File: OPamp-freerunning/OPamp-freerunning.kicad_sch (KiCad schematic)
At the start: 5 parts, among them U1 ${SIM.PARAMS}

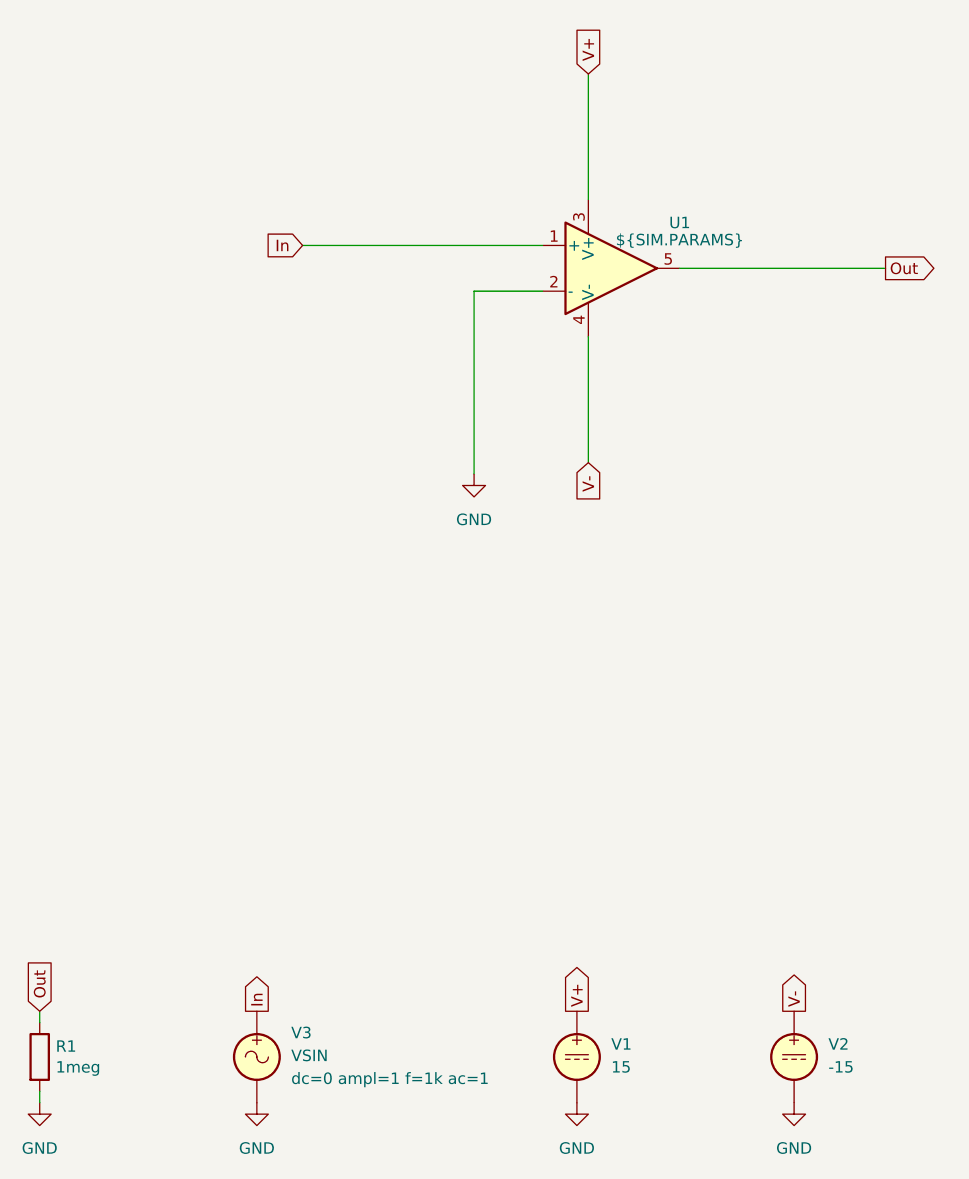
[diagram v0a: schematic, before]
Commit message: Tested/updated for KiCad 9
Schematics are tested and updated for KiCad 9, no changes in circuitry
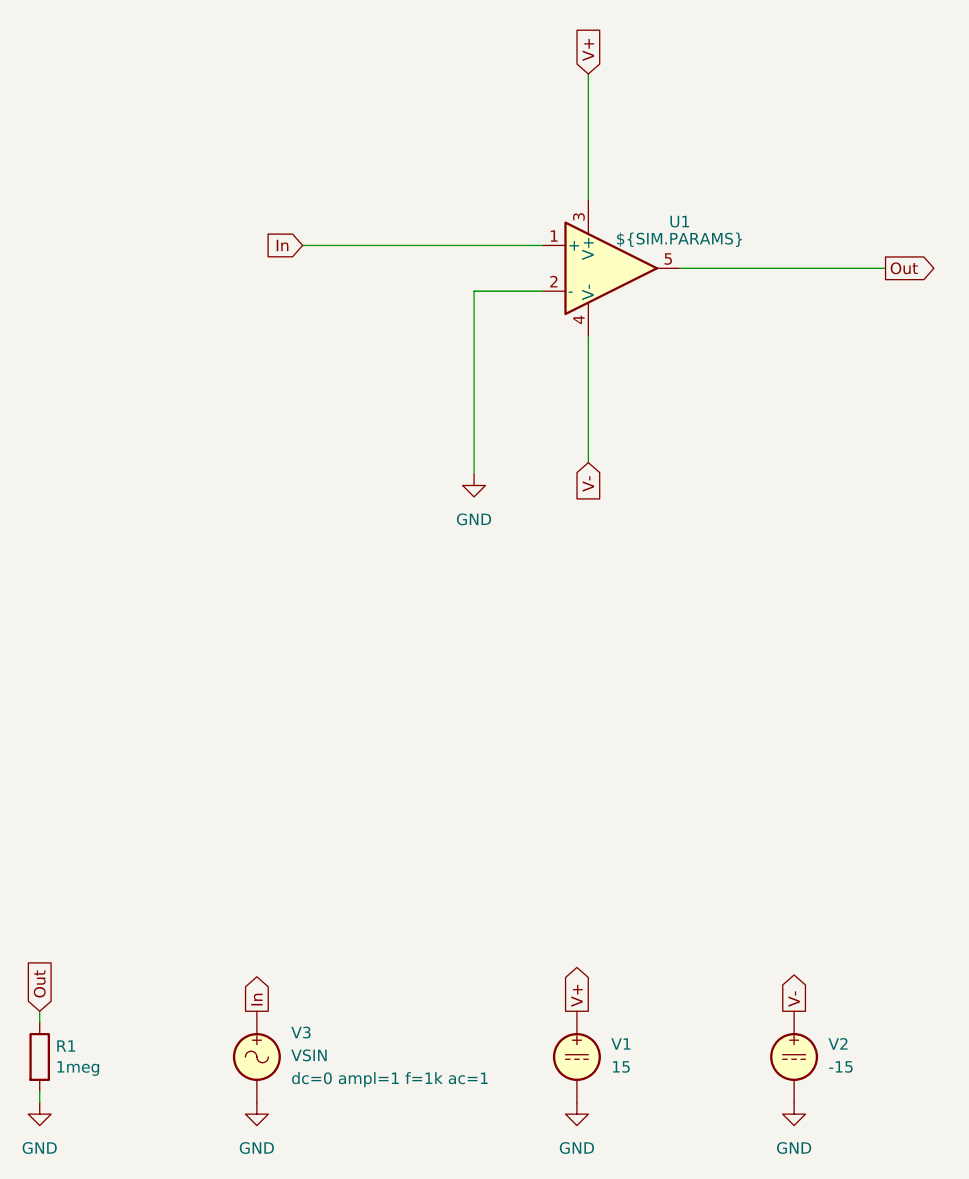
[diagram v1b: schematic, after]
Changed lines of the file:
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@@
 (kicad_sch
-	(version 20231120)
+	(version 20250114)
 	(generator "eeschema")
-	(generator_version "8.0")
+	(generator_version "9.0")
 	(paper "A4")
 	(title_block
 		(title "OPamp, freerunning")
-		(date "2024-12-15")
+		(date "2025-09-13")
 		(company "GitHub/OJStuff")
 		(comment 4 "Does not work properly at the time (probably built-in SPICE model problems)")
@@
 	)
 	(symbol
-		(lib_id "Simulation_SPICE:OPAMP")
-		(at 139.7 93.98 0)
-		(unit 1)
-		(exclude_from_sim no)
-		(in_bom yes)
-		(on_board yes)
-		(dnp no)
-		(fields_autoplaced yes)
-		(property "Reference" "U1"
-			(at 147.32 88.9314 0)
-			(effects
-				(font
-					(size 1.27 1.27)
-				)
-			)
-		)
-		(property "Value" "${SIM.PARAMS}"
-			(at 147.32 90.8365 0)
-			(effects
-				(font
-					(size 1.27 1.27)
-				)
-			)
-		)
-		(property "Footprint" ""
-			(at 139.7 93.98 0)
-			(effects
-				(font
-					(size 1.27 1.27)
-				)
-				(hide yes)
-			)
-		)
-		(property "Datasheet" "https://ngspice.sourceforge.io/docs/ngspice-html-manual/manual.xhtml#sec__SUBCKT_Subcircuits"
-			(at 139.7 93.98 0)
-			(effects
-				(font
-					(size 1.27 1.27)
-				)
-				(hide yes)
-			)
-		)
-		(property "Description" "Operational amplifier, single, node sequence=1:+ 2:- 3:OUT 4:V+ 5:V-"
-			(at 139.7 93.98 0)
-			(effects
-				(font
-					(size 1.27 1.27)
-				)
-				(hide yes)
-			)
-		)
-		(property "Sim.Pins" "1=in+ 2=in- 3=vcc 4=vee 5=out"
-			(at 139.7 93.98 0)
-			(effects
-				(font
-					(size 1.27 1.27)
-				)
-				(hide yes)
-			)
-		)
-		(property "Sim.Device" "SUBCKT"
-			(at 139.7 93.98 0)
-			(effects
-				(font
-					(size 1.27 1.27)
-				)
-				(justify left)
-				(hide yes)
-			)
-		)
-		(property "Sim.Library" "${KICAD8_SYMBOL_DIR}/Simulation_SPICE.sp"
-			(at 139.7 93.98 0)
-			(effects
-				(font
-					(size 1.27 1.27)
-				)
-				(hide yes)
-			)
-		)
-		(property "Sim.Name" "kicad_builtin_opamp"
-			(at 139.7 93.98 0)
-			(effects
-				(font
-					(size 1.27 1.27)
-				)
-				(hide yes)
-			)
-		)
-		(pin "2"
-		)
-		(pin "1"
-		)
-		(pin "5"
-		)
-		(pin "3"
-		)
-		(pin "4"
-		)
-		(instances
-			(project ""
-				(path "/d4e8d3f6-5bf3-42e6-a3b5-7574d3319bb2"
-					(reference "U1")
-					(unit 1)
-				)
-			)
-		)
-	)
-	(symbol
 		(lib_name "VDC_1")
 		(lib_id "Simulation_SPICE:VDC")
@@
 				(path "/d4e8d3f6-5bf3-42e6-a3b5-7574d3319bb2"
 					(reference "#PWR01")
+					(unit 1)
+				)
+			)
+		)
+	)
+	(symbol
+		(lib_id "Simulation_SPICE:OPAMP")
+		(at 139.7 93.98 0)
+		(unit 1)
+		(exclude_from_sim no)
+		(in_bom yes)
+		(on_board yes)
+		(dnp no)
+		(fields_autoplaced yes)
+		(property "Reference" "U1"
+			(at 147.32 88.8298 0)
+			(effects
+				(font
+					(size 1.27 1.27)
+				)
+			)
+		)
+		(property "Value" "${SIM.PARAMS}"
+			(at 147.32 90.7349 0)
+			(effects
+				(font
+					(size 1.27 1.27)
+				)
+			)
+		)
+		(property "Footprint" ""
+			(at 139.7 93.98 0)
+			(effects
+				(font
+					(size 1.27 1.27)
+				)
+				(hide yes)
+			)
+		)
+		(property "Datasheet" "https://ngspice.sourceforge.io/docs/ngspice-html-manual/manual.xhtml#sec__SUBCKT_Subcircuits"
+			(at 139.7 93.98 0)
+			(effects
+				(font
+					(size 1.27 1.27)
+				)
+				(hide yes)
+			)
+		)
+		(property "Description" "Operational amplifier, single"
+			(at 139.7 93.98 0)
+			(effects
+				(font
+					(size 1.27 1.27)
+				)
+				(hide yes)
+			)
+		)
+		(property "Sim.Pins" "1=in+ 2=in- 3=vcc 4=vee 5=out"
+			(at 139.7 93.98 0)
+			(effects
+				(font
+					(size 1.27 1.27)
+				)
+				(hide yes)
+			)
+		)
+		(property "Sim.Device" "SUBCKT"
+			(at 139.7 93.98 0)
+			(effects
+				(font
+					(size 1.27 1.27)
+				)
+				(justify left)
+				(hide yes)
+			)
+		)
+		(property "Sim.Library" "${KICAD9_SYMBOL_DIR}/Simulation_SPICE.sp"
+			(at 139.7 93.98 0)
+			(effects
+				(font
+					(size 1.27 1.27)
+				)
+				(hide yes)
+			)
+		)
+		(property "Sim.Name" "kicad_builtin_opamp"
+			(at 139.7 93.98 0)
+			(effects
+				(font
+					(size 1.27 1.27)
+				)
+				(hide yes)
+			)
+		)
+		(pin "5"
+		)
+		(pin "4"
+		)
+		(pin "3"
+		)
+		(pin "1"
+		)
+		(pin "2"
+		)
+		(instances
+			(project ""
+				(path "/d4e8d3f6-5bf3-42e6-a3b5-7574d3319bb2"
+					(reference "U1")
 					(unit 1)
 				)
@@
 		)
 	)
+	(embedded_fonts no)
 )
